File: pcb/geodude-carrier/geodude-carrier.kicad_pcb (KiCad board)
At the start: 2 copper layers, 140 x 134 mm, 43 parts, among them J1 12V, J2 12V, J3 GND, J31 SCL, J32 SDA, J34 3V3, J37 5V, J39 GND_L, J4 GND, J40 SCL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

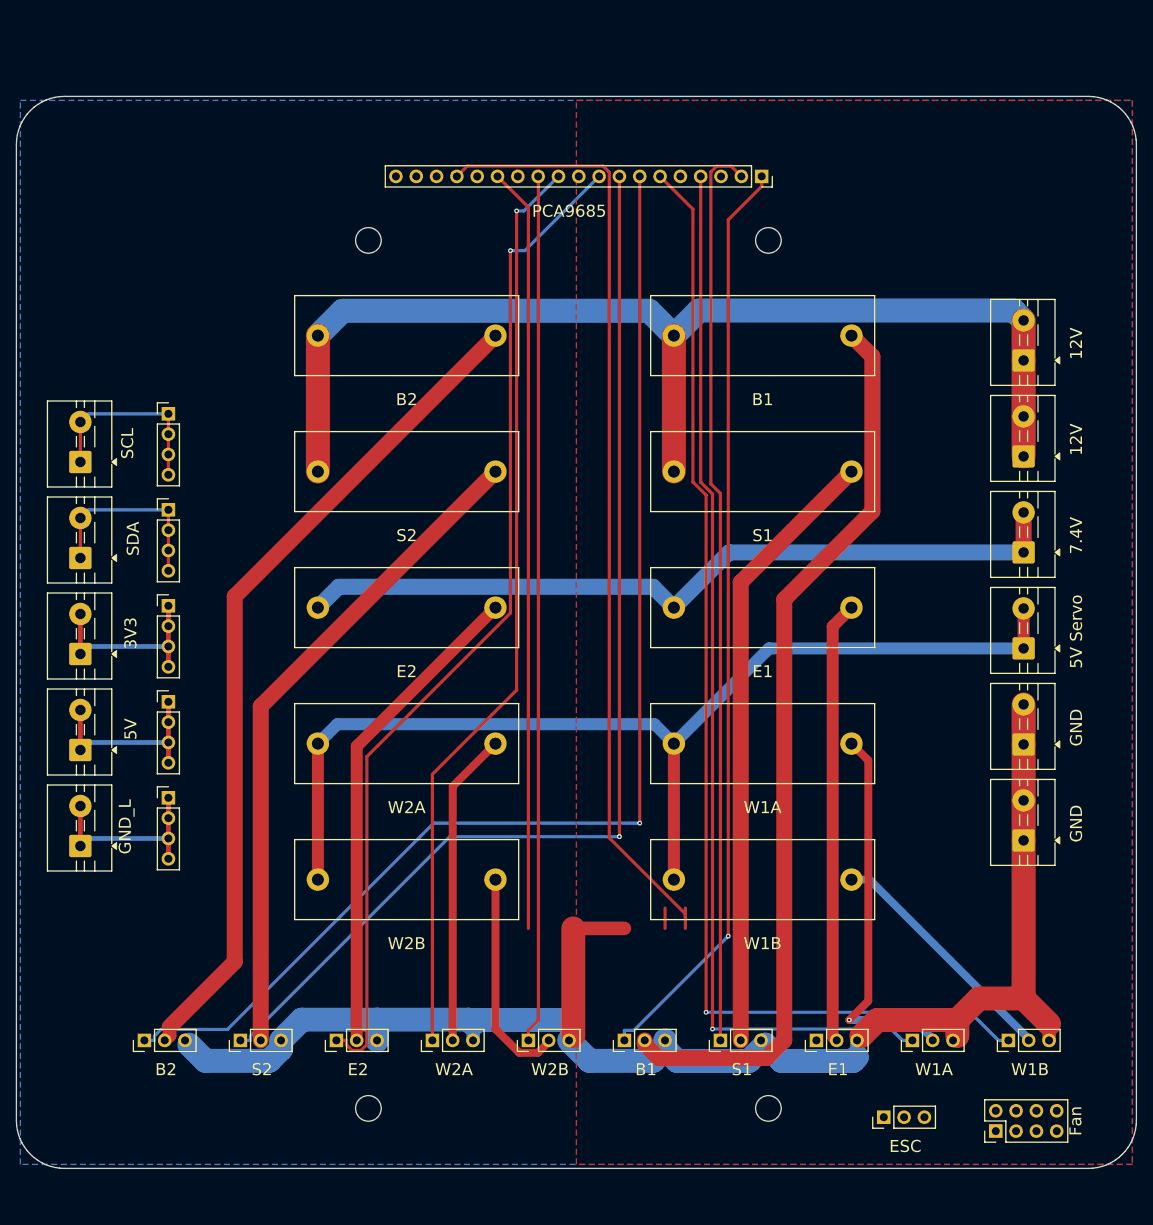
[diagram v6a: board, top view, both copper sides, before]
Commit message: Fully routed 242 tracks, 0 unconnected, 1 silk warning, Gerbers ready
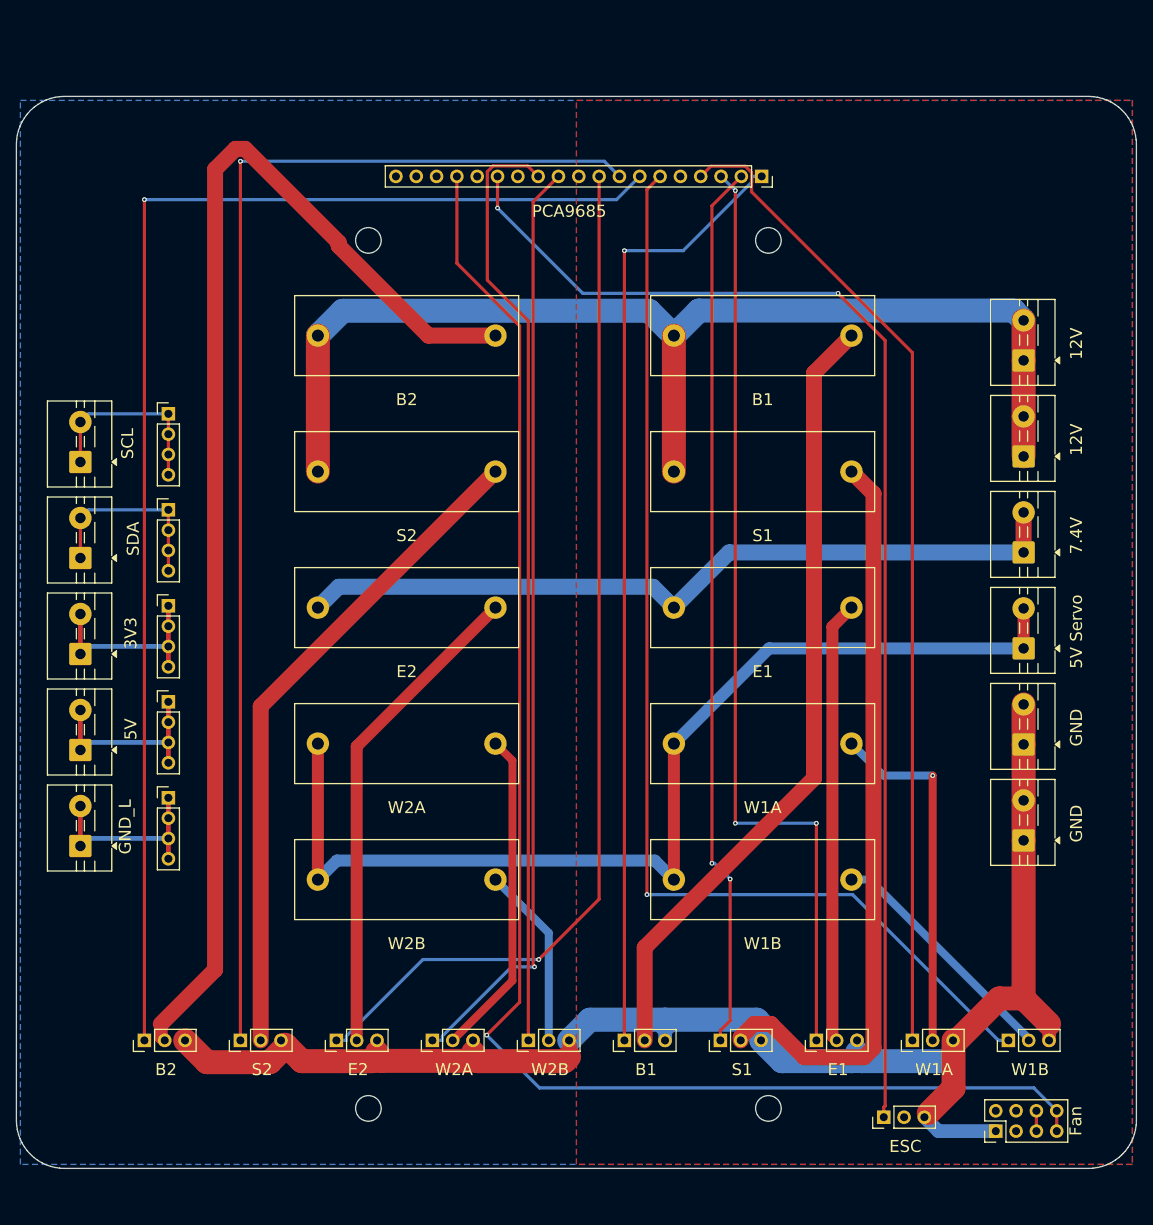
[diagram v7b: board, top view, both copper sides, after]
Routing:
- net PWM_CH2: track 0.00 -> 118.9 mm, vias 0 -> 3
- net PWM_CH12: track 119.6 -> 190.0 mm, vias 0 -> 1
- net PWM_CH11: track 95.6 -> 156.4 mm, vias 0 -> 2
- net SV6_PWR: track 105.2 -> 157.9 mm
- net PWM_CH6: track 140.8 -> 158.1 mm
- net SV2_PWR: track 76.8 -> 93.0 mm
- net SV1_PWR: track 113.3 -> 98.8 mm
- net PWM_CH5: track 154.3 -> 168.2 mm
- net PWM_CH9: track 108.5 -> 117.9 mm
- net PWM_CH3: track 132.8 -> 124.0 mm, vias 1 -> 0
- net SV10_PWR: track 27.3 -> 22.9 mm
- net PWM_CH0: track 115.8 -> 120.1 mm
- net PWM_CH7: track 126.6 -> 130.8 mm
- net SV4_PWR: track 48.0 -> 44.9 mm
- net PWM_CH4: track 146.1 -> 143.2 mm
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
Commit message: Add SimpleFOC system: Pi Pico, FOC driver, motor UVW, IMU, encoder, serial link. Remove ESC.
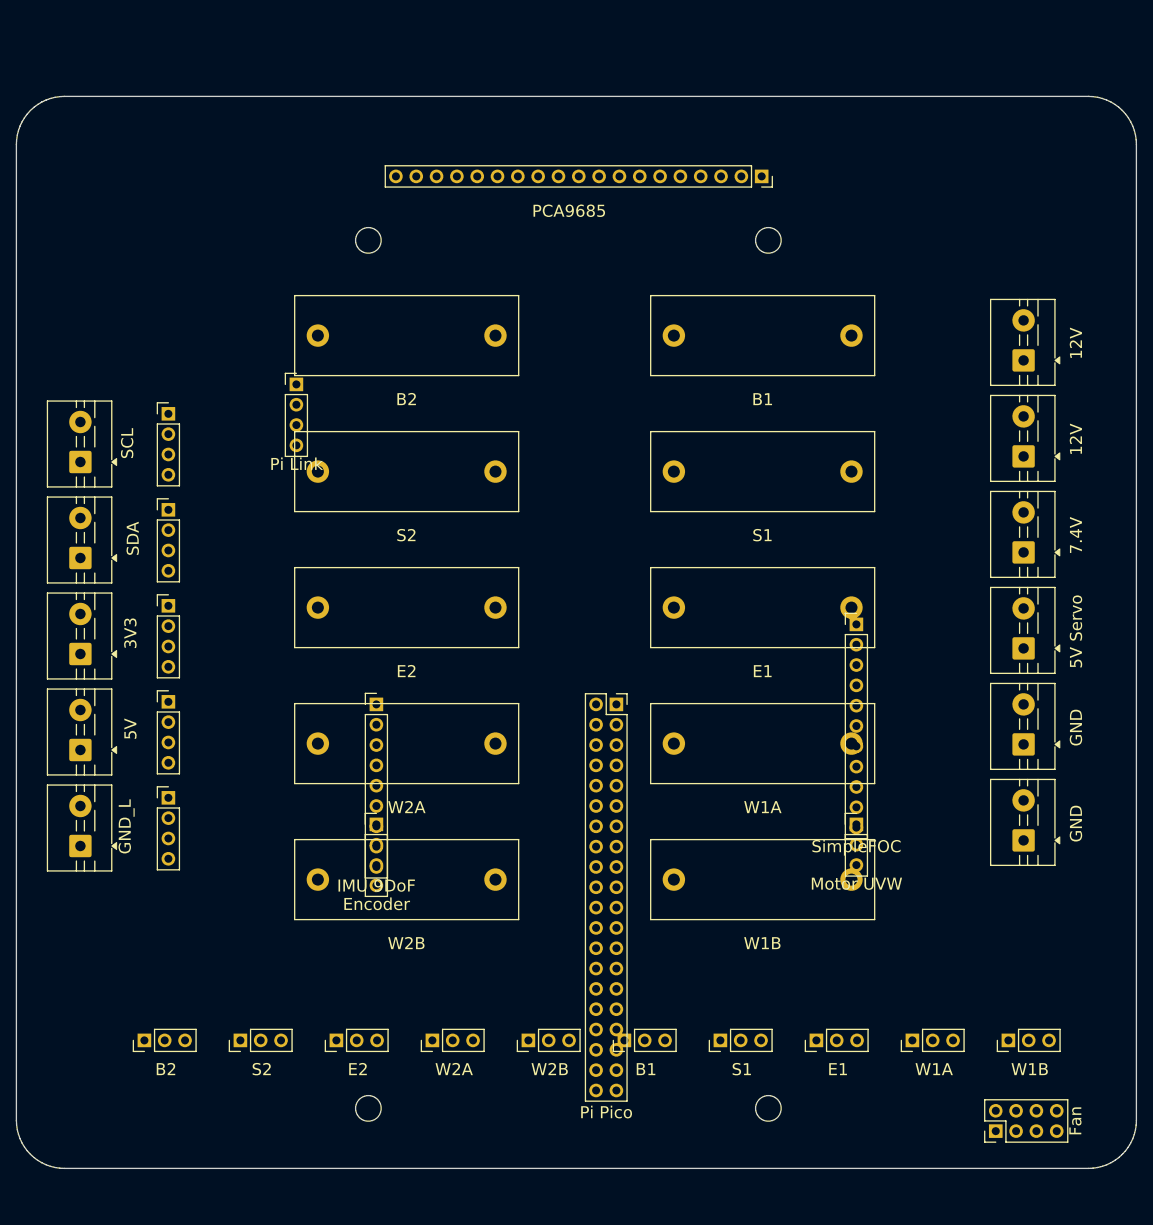
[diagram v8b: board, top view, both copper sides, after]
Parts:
- removed J_ESC: ESC, PinHeader_1x03_P2.54mm_Vertical
- added J_ENC: Encoder, PinHeader_1x04_P2.54mm_Vertical, F.Cu at (50.0, 105.0)
- added J_FOC: SimpleFOC, PinHeader_1x11_P2.54mm_Vertical, F.Cu at (110.0, 80.0)
- added J_IMU: IMU 9DoF, PinHeader_1x09_P2.54mm_Vertical, F.Cu at (50.0, 90.0)
- added J_MOTOR: Motor UVW, PinHeader_1x03_P2.54mm_Vertical, F.Cu at (110.0, 105.0)
- added J_PICO: Pi Pico, PinSocket_2x20_P2.54mm_Vertical, F.Cu at (80.0, 90.0)
- added J_SERIAL: Pi Link, PinHeader_1x04_P2.54mm_Vertical, F.Cu at (40.0, 50.0)
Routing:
- net GND: track 193.9 -> 0.00 mm
- net PWM_CH12: track 190.0 -> 0.00 mm, vias 1 -> 0
- net PWM_CH5: track 168.2 -> 0.00 mm, vias 1 -> 0
- net PWM_CH6: track 158.1 -> 0.00 mm, vias 1 -> 0
- net SV6_PWR: track 157.9 -> 0.00 mm
- net PWM_CH11: track 156.4 -> 0.00 mm, vias 2 -> 0
- net +12V: track 143.6 -> 0.00 mm
- net PWM_CH4: track 143.2 -> 0.00 mm, vias 1 -> 0
- net +5V_SERVO: track 134.1 -> 0.00 mm
- net PWM_CH7: track 130.8 -> 0.00 mm, vias 1 -> 0
- net PWM_CH3: track 124.0 -> 0.00 mm
- net PWM_CH0: track 120.1 -> 0.00 mm, vias 1 -> 0
- net PWM_CH2: track 118.9 -> 0.00 mm, vias 3 -> 0
- net PWM_CH9: track 117.9 -> 0.00 mm
- net PWM_CH8: track 117.1 -> 0.00 mm, vias 1 -> 0
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- removed copper zone on F.Cu, net +12V
- removed copper zone on B.Cu, net GND
